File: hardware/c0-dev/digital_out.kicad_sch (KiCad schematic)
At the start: 41 parts, among them Q1001 BSS138P, Q1002 BSS138P, Q1003 BSS138P, Q1004 BSS138P, Q1005 BSS138P, Q1006 BSS138P, Q1007 BSS138P, Q1008 BSS138P, Q1009 BSS138P, U1001 TCA9555PWR, U1002 TPS4H000A-Q1, U1003 TPS4H000A-Q1

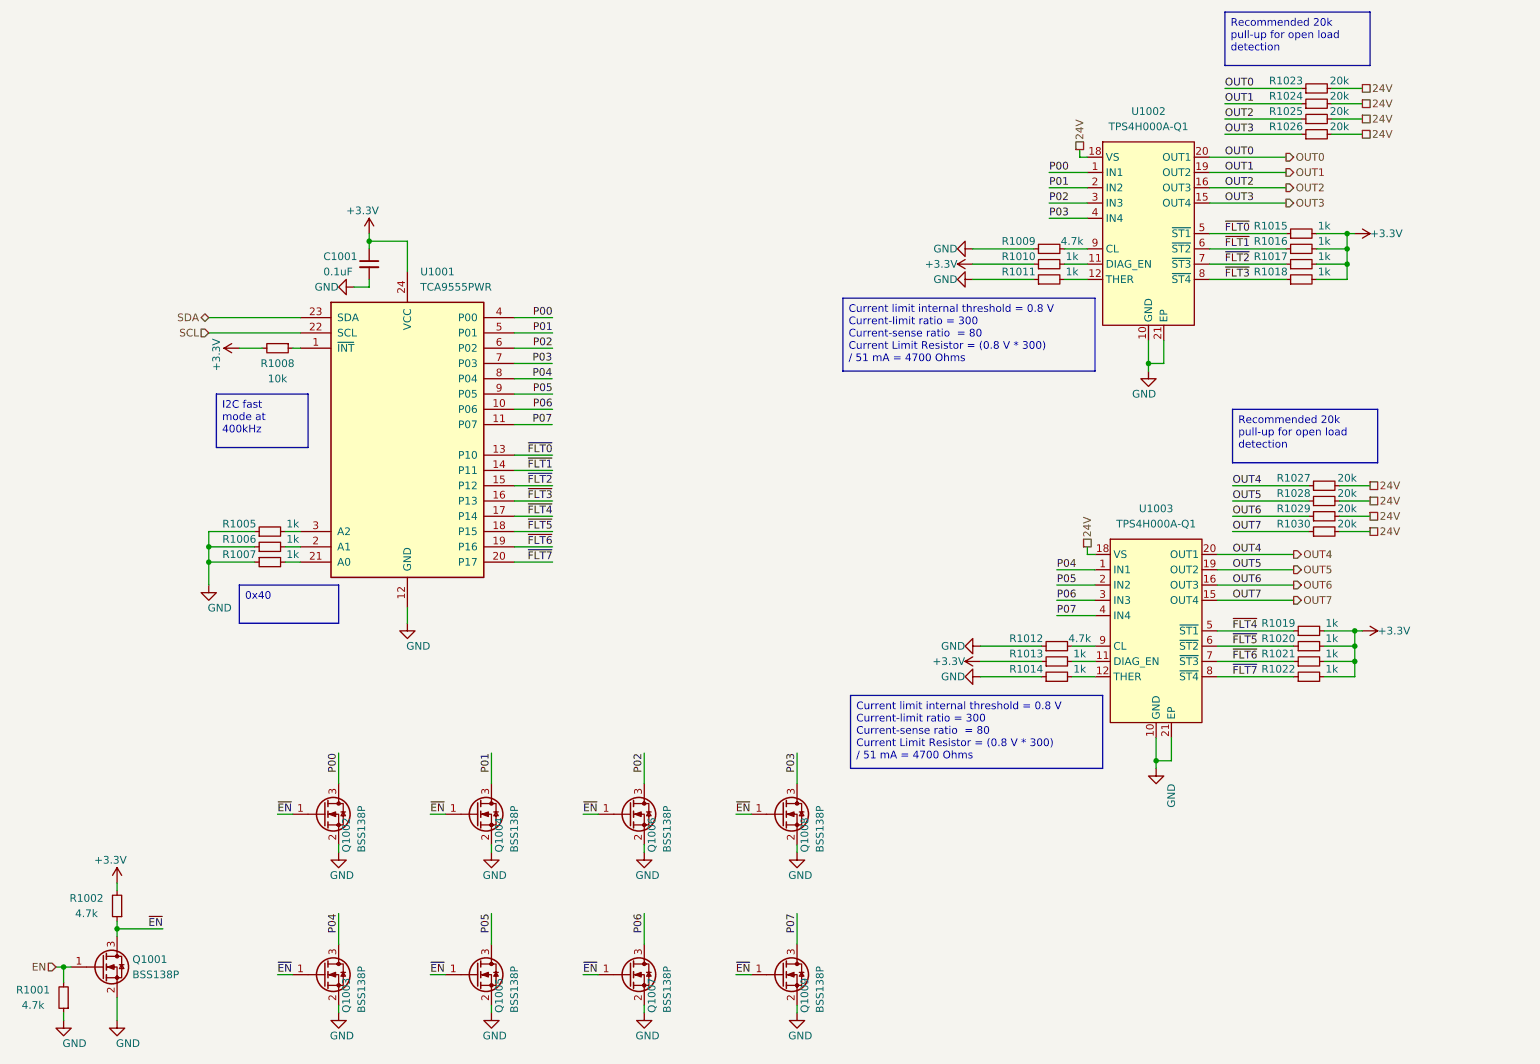
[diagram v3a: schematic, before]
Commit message: added leds, removed screen
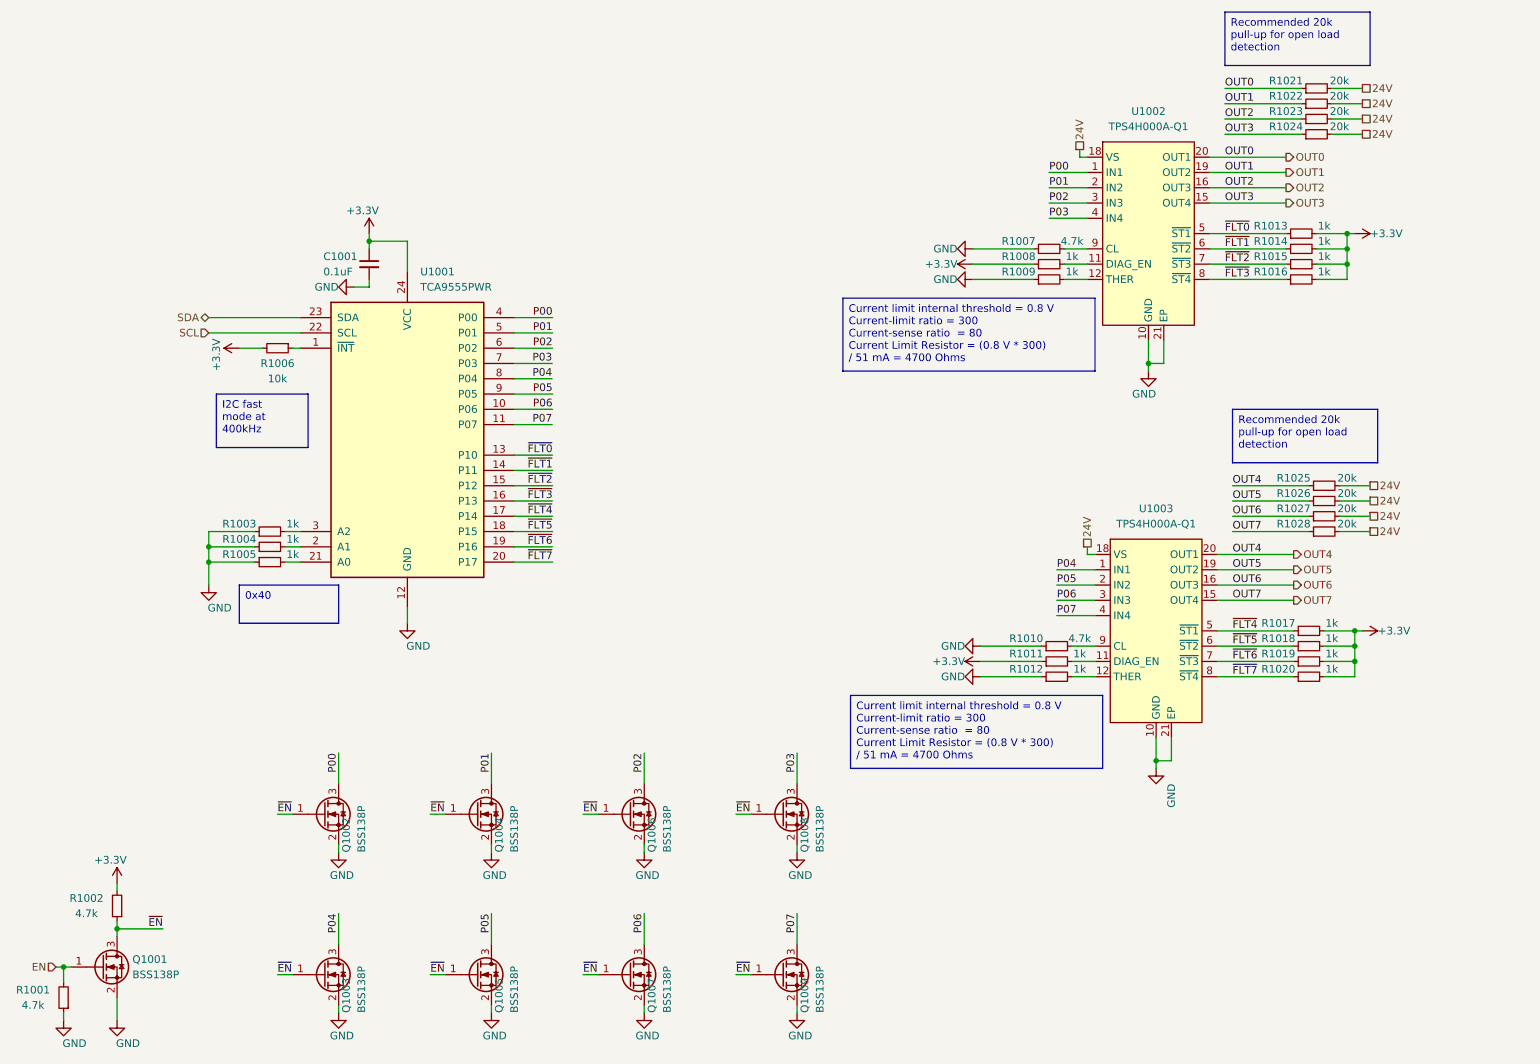
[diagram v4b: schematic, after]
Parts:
- renumbered R1005 to R1003, R1006 to R1004, R1007 to R1005, R1008 to R1006, R1009 to R1007, R1010 to R1008, R1011 to R1009, R1012 to R1010, R1013 to R1011, R1014 to R1012, R1015 to R1013, R1016 to R1014, R1017 to R1015, R1018 to R1016, R1019 to R1017, R1020 to R1018, R1021 to R1019, R1022 to R1020, R1023 to R1021, R1024 to R1022, R1025 to R1023, R1026 to R1024, R1027 to R1025, R1028 to R1026, R1029 to R1027, R1030 to R1028
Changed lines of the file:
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@@
 		(in_pos_files yes)
 		(dnp no)
-		(property "Reference" "R1018"
+		(property "Reference" "R1016"
 			(at 236.22 59.69 90)
 			(show_name no)
@@
 			(project "c0-dev"
 				(path "/b8347a0e-ad04-4414-969d-3c64a611d74e/680032e3-5da4-48ad-9c49-e468cbbeffb9"
-					(reference "R1018")
+					(reference "R1016")
 					(unit 1)
 				)
@@
 		(in_pos_files yes)
 		(dnp no)
-		(property "Reference" "R1029"
+		(property "Reference" "R1027"
 			(at 240.03 99.06 90)
 			(show_name no)
@@
 			(project "c0-dev"
 				(path "/b8347a0e-ad04-4414-969d-3c64a611d74e/680032e3-5da4-48ad-9c49-e468cbbeffb9"
-					(reference "R1029")
+					(reference "R1027")
 					(unit 1)
 				)
@@
 		(in_pos_files yes)
 		(dnp no)
-		(property "Reference" "R1015"
+		(property "Reference" "R1013"
 			(at 236.22 52.07 90)
 			(show_name no)
@@
 			(project "c0-dev"
 				(path "/b8347a0e-ad04-4414-969d-3c64a611d74e/680032e3-5da4-48ad-9c49-e468cbbeffb9"
-					(reference "R1015")
+					(reference "R1013")
 					(unit 1)
 				)
@@
 		(in_pos_files yes)
 		(dnp no)
-		(property "Reference" "R1005"
+		(property "Reference" "R1003"
 			(at 64.77 101.6 90)
 			(show_name no)
@@
 			(project "c0-dev"
 				(path "/b8347a0e-ad04-4414-969d-3c64a611d74e/680032e3-5da4-48ad-9c49-e468cbbeffb9"
-					(reference "R1005")
+					(reference "R1003")
 					(unit 1)
 				)
@@
 		(in_pos_files yes)
 		(dnp no)
-		(property "Reference" "R1008"
+		(property "Reference" "R1006"
 			(at 71.12 74.93 90)
 			(show_name no)
@@
 			(project "c0-dev"
 				(path "/b8347a0e-ad04-4414-969d-3c64a611d74e/680032e3-5da4-48ad-9c49-e468cbbeffb9"
-					(reference "R1008")
+					(reference "R1006")
 					(unit 1)
 				)
@@
 		(in_pos_files yes)
 		(dnp no)
-		(property "Reference" "R1013"
+		(property "Reference" "R1011"
 			(at 195.58 123.19 90)
 			(show_name no)
@@
 			(project "c0-dev"
 				(path "/b8347a0e-ad04-4414-969d-3c64a611d74e/680032e3-5da4-48ad-9c49-e468cbbeffb9"
-					(reference "R1013")
+					(reference "R1011")
 					(unit 1)
 				)
@@
 		(in_pos_files yes)
 		(dnp no)
-		(property "Reference" "R1010"
+		(property "Reference" "R1008"
 			(at 194.31 57.15 90)
 			(show_name no)
@@
 			(project "c0-dev"
 				(path "/b8347a0e-ad04-4414-969d-3c64a611d74e/680032e3-5da4-48ad-9c49-e468cbbeffb9"
-					(reference "R1010")
+					(reference "R1008")
 					(unit 1)
 				)
@@
 		(in_pos_files yes)
 		(dnp no)
-		(property "Reference" "R1020"
+		(property "Reference" "R1018"
 			(at 237.49 120.65 90)
 			(show_name no)
@@
 			(project "c0-dev"
 				(path "/b8347a0e-ad04-4414-969d-3c64a611d74e/680032e3-5da4-48ad-9c49-e468cbbeffb9"
-					(reference "R1020")
+					(reference "R1018")
 					(unit 1)
 				)
@@
 		(in_pos_files yes)
 		(dnp no)
-		(property "Reference" "R1007"
+		(property "Reference" "R1005"
 			(at 64.77 106.68 90)
 			(show_name no)
@@
 			(project "c0-dev"
 				(path "/b8347a0e-ad04-4414-969d-3c64a611d74e/680032e3-5da4-48ad-9c49-e468cbbeffb9"
-					(reference "R1007")
+					(reference "R1005")
 					(unit 1)
 				)
@@
 		(in_pos_files yes)
 		(dnp no)
-		(property "Reference" "R1022"
+		(property "Reference" "R1020"
 			(at 237.49 125.73 90)
 			(show_name no)
@@
 			(project "c0-dev"
 				(path "/b8347a0e-ad04-4414-969d-3c64a611d74e/680032e3-5da4-48ad-9c49-e468cbbeffb9"
-					(reference "R1022")
+					(reference "R1020")
 					(unit 1)
 				)
@@
 		(in_pos_files yes)
 		(dnp no)
-		(property "Reference" "R1026"
+		(property "Reference" "R1024"
 			(at 238.76 35.56 90)
 			(show_name no)
@@
 			(project "c0-dev"
 				(path "/b8347a0e-ad04-4414-969d-3c64a611d74e/680032e3-5da4-48ad-9c49-e468cbbeffb9"
-					(reference "R1026")
+					(reference "R1024")
 					(unit 1)
 				)
@@
 		(in_pos_files yes)
 		(dnp no)
-		(property "Reference" "R1011"
+		(property "Reference" "R1009"
 			(at 194.31 59.69 90)
 			(show_name no)
@@
 			(project "c0-dev"
 				(path "/b8347a0e-ad04-4414-969d-3c64a611d74e/680032e3-5da4-48ad-9c49-e468cbbeffb9"
-					(reference "R1011")
+					(reference "R1009")
 					(unit 1)
 				)
@@
 		(in_pos_files yes)
 		(dnp no)
-		(property "Reference" "R1016"
+		(property "Reference" "R1014"
 			(at 236.22 54.61 90)
 			(show_name no)
@@
 			(project "c0-dev"
 				(path "/b8347a0e-ad04-4414-969d-3c64a611d74e/680032e3-5da4-48ad-9c49-e468cbbeffb9"
-					(reference "R1016")
+					(reference "R1014")
 					(unit 1)
 				)
@@
 		(in_pos_files yes)
 		(dnp no)
-		(property "Reference" "R1030"
+		(property "Reference" "R1028"
 			(at 240.03 101.6 90)
 			(show_name no)
@@
 			(project "c0-dev"
 				(path "/b8347a0e-ad04-4414-969d-3c64a611d74e/680032e3-5da4-48ad-9c49-e468cbbeffb9"
-					(reference "R1030")
+					(reference "R1028")
 					(unit 1)
 				)
@@
 		(in_pos_files yes)
 		(dnp no)
-		(property "Reference" "R1006"
+		(property "Reference" "R1004"
 			(at 64.77 104.14 90)
 			(show_name no)
@@
 			(project "c0-dev"
 				(path "/b8347a0e-ad04-4414-969d-3c64a611d74e/680032e3-5da4-48ad-9c49-e468cbbeffb9"
-					(reference "R1006")
+					(reference "R1004")
 					(unit 1)
 				)
@@
 		(in_pos_files yes)
 		(dnp no)
-		(property "Reference" "R1023"
+		(property "Reference" "R1021"
 			(at 238.76 27.94 90)
 			(show_name no)
@@
 			(project "c0-dev"
 				(path "/b8347a0e-ad04-4414-969d-3c64a611d74e/680032e3-5da4-48ad-9c49-e468cbbeffb9"
-					(reference "R1023")
+					(reference "R1021")
 					(unit 1)
 				)
@@
 		(in_pos_files yes)
 		(dnp no)
-		(property "Reference" "R1028"
+		(property "Reference" "R1026"
 			(at 240.03 96.52 90)
 			(show_name no)
@@
 			(project "c0-dev"
 				(path "/b8347a0e-ad04-4414-969d-3c64a611d74e/680032e3-5da4-48ad-9c49-e468cbbeffb9"
-					(reference "R1028")
+					(reference "R1026")
 					(unit 1)
 				)
@@
 		(in_pos_files yes)
 		(dnp no)
-		(property "Reference" "R1012"
+		(property "Reference" "R1010"
 			(at 195.58 120.65 90)
 			(show_name no)
@@
 			(project "c0-dev"
 				(path "/b8347a0e-ad04-4414-969d-3c64a611d74e/680032e3-5da4-48ad-9c49-e468cbbeffb9"
-					(reference "R1012")
+					(reference "R1010")
 					(unit 1)
 				)
@@
 		(in_pos_files yes)
 		(dnp no)
-		(property "Reference" "R1024"
+		(property "Reference" "R1022"
 			(at 238.76 30.48 90)
 			(show_name no)
@@
 			(project "c0-dev"
 				(path "/b8347a0e-ad04-4414-969d-3c64a611d74e/680032e3-5da4-48ad-9c49-e468cbbeffb9"
-					(reference "R1024")
+					(reference "R1022")
 					(unit 1)
 				)
@@
 		(in_pos_files yes)
 		(dnp no)
-		(property "Reference" "R1027"
+		(property "Reference" "R1025"
 			(at 240.03 93.98 90)
 			(show_name no)
@@
 			(project "c0-dev"
 				(path "/b8347a0e-ad04-4414-969d-3c64a611d74e/680032e3-5da4-48ad-9c49-e468cbbeffb9"
-					(reference "R1027")
+					(reference "R1025")
 					(unit 1)
 				)
@@
 		(in_pos_files yes)
 		(dnp no)
-		(property "Reference" "R1009"
+		(property "Reference" "R1007"
 			(at 194.31 54.61 90)
 			(show_name no)
@@
 			(project "c0-dev"
 				(path "/b8347a0e-ad04-4414-969d-3c64a611d74e/680032e3-5da4-48ad-9c49-e468cbbeffb9"
-					(reference "R1009")
+					(reference "R1007")
 					(unit 1)
 				)
@@
 		(in_pos_files yes)
 		(dnp no)
-		(property "Reference" "R1019"
+		(property "Reference" "R1017"
 			(at 237.49 118.11 90)
 			(show_name no)
@@
 			(project "c0-dev"
 				(path "/b8347a0e-ad04-4414-969d-3c64a611d74e/680032e3-5da4-48ad-9c49-e468cbbeffb9"
-					(reference "R1019")
+					(reference "R1017")
 					(unit 1)
 				)
@@
 		(in_pos_files yes)
 		(dnp no)
-		(property "Reference" "R1014"
+		(property "Reference" "R1012"
 			(at 195.58 125.73 90)
 			(show_name no)
@@
 			(project "c0-dev"
 				(path "/b8347a0e-ad04-4414-969d-3c64a611d74e/680032e3-5da4-48ad-9c49-e468cbbeffb9"
-					(reference "R1014")
+					(reference "R1012")
 					(unit 1)
 				)
@@
 		(in_pos_files yes)
 		(dnp no)
-		(property "Reference" "R1017"
+		(property "Reference" "R1015"
 			(at 236.22 57.15 90)
 			(show_name no)
@@
 			(project "c0-dev"
 				(path "/b8347a0e-ad04-4414-969d-3c64a611d74e/680032e3-5da4-48ad-9c49-e468cbbeffb9"
-					(reference "R1017")
+					(reference "R1015")
 					(unit 1)
 				)
@@
 		(in_pos_files yes)
 		(dnp no)
-		(property "Reference" "R1021"
+		(property "Reference" "R1019"
 			(at 237.49 123.19 90)
 			(show_name no)
@@
 			(project "c0-dev"
 				(path "/b8347a0e-ad04-4414-969d-3c64a611d74e/680032e3-5da4-48ad-9c49-e468cbbeffb9"
-					(reference "R1021")
+					(reference "R1019")
 					(unit 1)
 				)
@@
 		(in_pos_files yes)
 		(dnp no)
-		(property "Reference" "R1025"
+		(property "Reference" "R1023"
 			(at 238.76 33.02 90)
 			(show_name no)
@@
 			(project "c0-dev"
 				(path "/b8347a0e-ad04-4414-969d-3c64a611d74e/680032e3-5da4-48ad-9c49-e468cbbeffb9"
-					(reference "R1025")
+					(reference "R1023")
 					(unit 1)
 				)
